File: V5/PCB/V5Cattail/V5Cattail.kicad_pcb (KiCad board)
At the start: 2 copper layers, 10.9 x 31.1 mm, 10 parts, among them U1 ST-0277D00-052-142, U2 SRV05-4_C558418, U3 BMI270

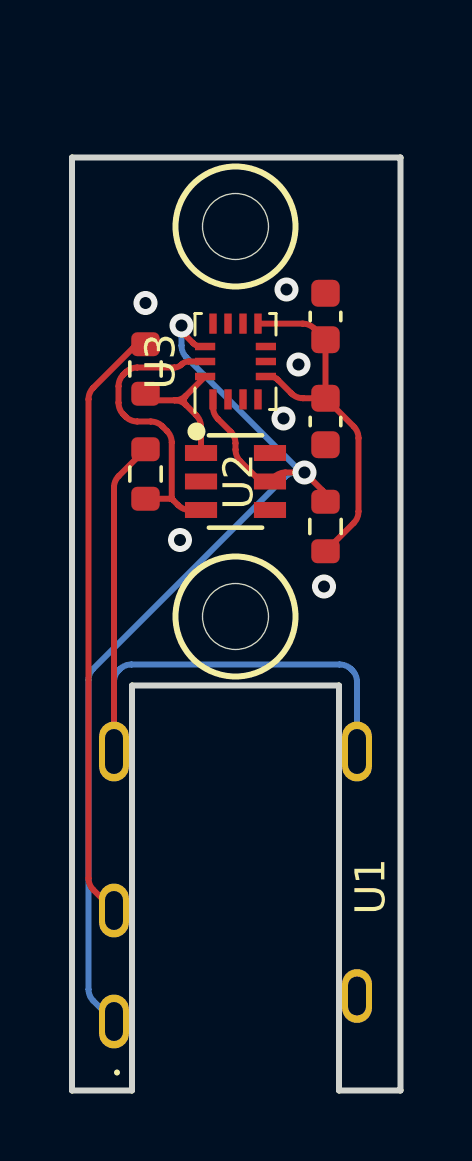
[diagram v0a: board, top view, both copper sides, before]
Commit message: reorganizing CAD files
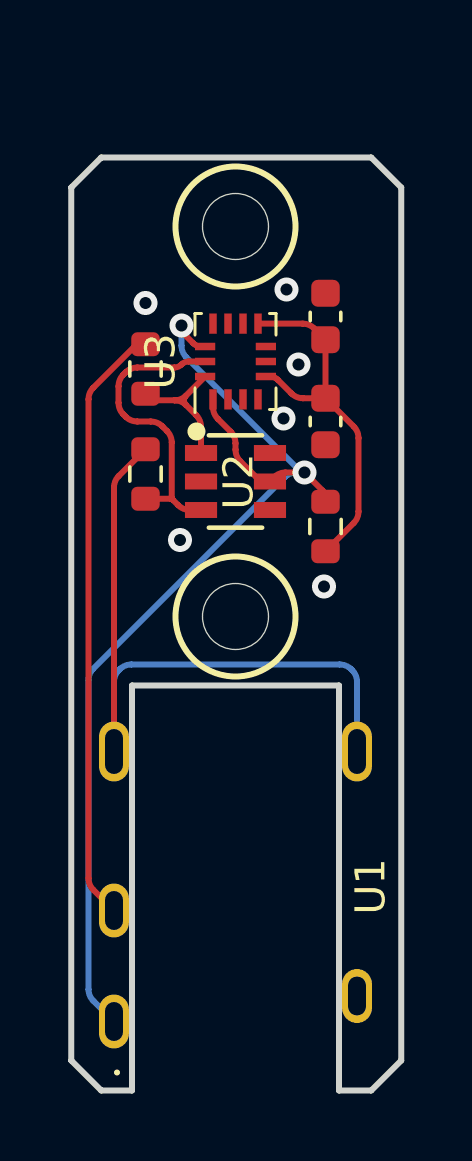
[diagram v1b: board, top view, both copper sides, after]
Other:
- board size 10.9 x 31.1 mm -> 11 x 31.1 mm
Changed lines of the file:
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@@
   (gr_circle (center 147 97) (end 148.99999 96.999991)
     (stroke (width 0.2) (type solid)) (fill none) (layer "F.SilkS"))
-  (gr_line (start 143.55 112.8) (end 143.55 99.3)
-    (stroke (width 0.2) (type default)) (layer "Edge.Cuts"))
-  (gr_line (start 150.45 112.8) (end 152.5 112.8)
-    (stroke (width 0.2) (type default)) (layer "Edge.Cuts"))
+  (gr_line (start 152.525 82.7) (end 151.525 81.7)
+    (stroke (width 0.2) (type solid)) (layer "Edge.Cuts"))
   (gr_line (start 143.55 112.8) (end 143.55 112.8)
     (stroke (width 0.2) (type default)) (layer "Edge.Cuts"))
-  (gr_line (start 141.55 112.8) (end 143.55 112.8)
-    (stroke (width 0.2) (type default)) (layer "Edge.Cuts"))
-  (gr_line (start 152.5 81.7) (end 141.55 81.7)
-    (stroke (width 0.2) (type default)) (layer "Edge.Cuts"))
-  (gr_line (start 150.45 99.3) (end 150.45 112.8)
-    (stroke (width 0.2) (type default)) (layer "Edge.Cuts"))
-  (gr_line (start 141.55 81.7) (end 141.55 112.8)
-    (stroke (width 0.2) (type default)) (layer "Edge.Cuts"))
+  (gr_line (start 141.525 111.8) (end 142.525 112.8)
+    (stroke (width 0.2) (type solid)) (layer "Edge.Cuts"))
+  (gr_line (start 142.525 81.7) (end 141.525 82.7)
+    (stroke (width 0.2) (type solid)) (layer "Edge.Cuts"))
   (gr_line (start 143.55 99.3) (end 150.45 99.3)
-    (stroke (width 0.2) (type default)) (layer "Edge.Cuts"))
-  (gr_line (start 152.5 112.8) (end 152.5 81.7)
-    (stroke (width 0.2) (type default)) (layer "Edge.Cuts"))
+    (stroke (width 0.2) (type solid)) (layer "Edge.Cuts"))
+  (gr_line (start 150.45 112.8) (end 150.45 99.3)
+    (stroke (width 0.2) (type solid)) (layer "Edge.Cuts"))
+  (gr_line (start 141.525 111.8) (end 141.525 82.7)
+    (stroke (width 0.2) (type solid)) (layer "Edge.Cuts"))
+  (gr_line (start 142.525 81.7) (end 151.525 81.7)
+    (stroke (width 0.2) (type solid)) (layer "Edge.Cuts"))
+  (gr_line (start 142.525 112.8) (end 143.55 112.8)
+    (stroke (width 0.2) (type solid)) (layer "Edge.Cuts"))
+  (gr_line (start 143.55 112.8) (end 143.55 99.3)
+    (stroke (width 0.2) (type solid)) (layer "Edge.Cuts"))
+  (gr_line (start 150.45 112.8) (end 151.525 112.8)
+    (stroke (width 0.2) (type solid)) (layer "Edge.Cuts"))
+  (gr_line (start 152.525 111.8) (end 152.525 82.7)
+    (stroke (width 0.2) (type solid)) (layer "Edge.Cuts"))
+  (gr_line (start 152.525 111.8) (end 151.525 112.8)
+    (stroke (width 0.2) (type solid)) (layer "Edge.Cuts"))
   (segment (start 147.747143 92.392551) (end 147.76534 92.392551) (width 0.2) (layer "F.Cu") (net 1))
   (segment (start 149.902772 92.802772) (end 149.3 92.2) (width 0.2) (layer "F.Cu") (net 1))
@@
     (polygon
       (pts
+        (xy 142.525 112.8)
+        (xy 141.525 111.8)
+        (xy 141.525 82.7)
+        (xy 142.525 81.7)
+        (xy 151.525 81.7)
+        (xy 152.525 82.7)
+        (xy 152.525 111.8)
+        (xy 151.525 112.8)
         (xy 150.45 112.8)
         (xy 150.45 99.3)
         (xy 143.55 99.3)
         (xy 143.55 112.8)
-        (xy 141.55 112.8)
-        (xy 141.55 81.7)
-        (xy 152.5 81.7)
-        (xy 152.5 112.8)
-      )
-    )
+      )
+    )

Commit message: Overdue backup
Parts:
- removed ? (x2): , 
- removed R1, R2, R3: 1k, Resistor_SMD:R_0603_1608Metric
- C1, C2: value 100n -> 100nF; footprint Capacitor_SMD:C_0603_1608Metric -> LilypadVR:C_0603_1608Metric
- J1: renamed from U1; value ST-0277D00-052-142 -> TRRS; footprint AUDIO-TH_ST-0277D00-052-142:AUDIO-TH_ST-0277D00-052-142 -> LilypadVR:AUDIO-TH_ST-0277D00-052-142
- U1: renamed from U2; footprint SOT-23-6_L2.9-W1.6-P0.95-LS2.8-BL:SOT-23-6_L2.9-W1.6-P0.95-LS2.8-BL -> LilypadVR:SOT-23-6
- moved C1 6.99 mm to (144.4, 86.3), turned to 90 degrees
- moved C2 3.67 mm to (147.0, 89.1), turned to 0 degrees
- moved U2 2.21 mm to (147.0, 86.3), turned to -90 degrees
- moved U1 0.70 mm to (147.0, 91.8), turned to 180 degrees
- renumbered U3 to U2
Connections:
- C1 pad 1: Net-(U3-VDD) -> GND
- C1 pad 2: GND -> +3V3
- C2 pad 1: Net-(U3-VDD) -> +3V3
- J1 pad 3: Net-(R1-Pad2) -> SDA
- J1 pad 4: Net-(R2-Pad2) -> SCL
- J1 pad 5: Net-(R2-Pad2) -> SCL
- U1 pad 1: /SDA -> SDA
- U1 pad 3: /SCL -> SCL
- U2 pad 13: /SCL -> SCL
- U2 pad 14: /SDA -> SDA
- U2 pad 5: Net-(U3-VDD) -> +3V3
- U2 pad 8: Net-(U3-VDD) -> +3V3
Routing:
- net SCL: track 0.00 -> 28.9 mm, vias 0 -> 1
- net SDA: track 0.00 -> 27.5 mm
- net Net-(R2-Pad2): track 23.9 -> 0.00 mm
- net Net-(R1-Pad2): track 20.1 -> 0.00 mm
- net Net-(U3-VDD): track 12.6 -> 0.00 mm
- net /SCL: track 10.2 -> 0.00 mm
- net +3V3: track 35.3 -> 43.7 mm, vias 2 -> 1
- net /SDA: track 4.89 -> 0.00 mm
- net GND: vias 6 -> 32
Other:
- board size 11 x 31.1 mm -> 11 x 34 mm
- rule pad_to_mask_clearance: 0 -> 0.038

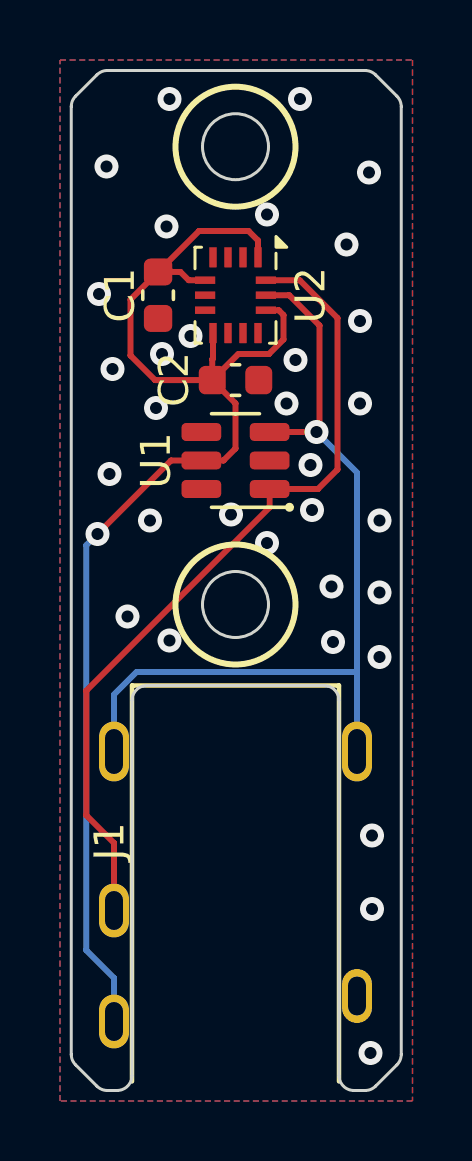
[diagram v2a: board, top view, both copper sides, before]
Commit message: Prototype Model/PCB Updates
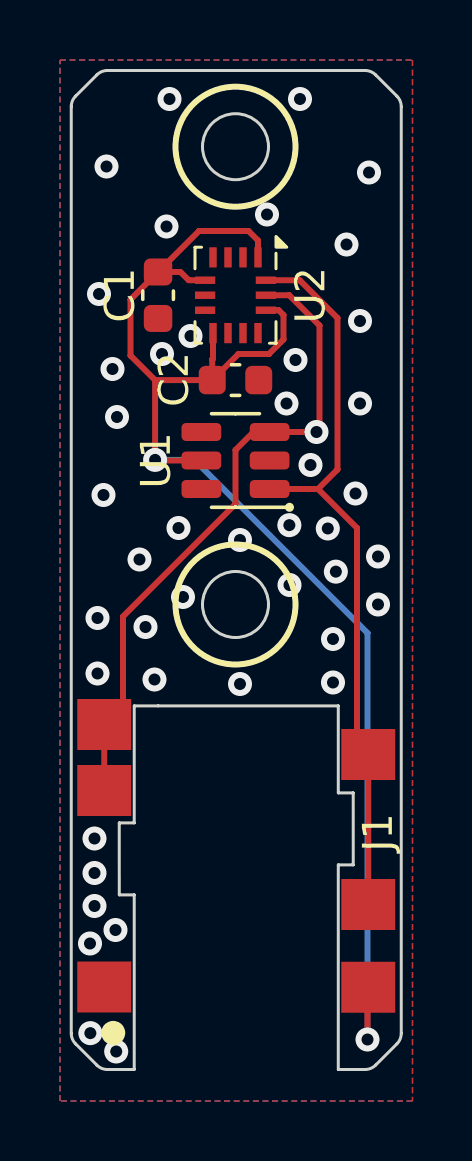
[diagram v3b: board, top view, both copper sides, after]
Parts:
- J1: footprint LilypadVR:AUDIO-TH_ST-0277D00-052-142 -> LilypadVR:AUDIO-SMD_PJ-342C
- moved J1 1.02 mm to (147.0, 105.0), turned to 180 degrees
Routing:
- net SCL: track 28.9 -> 21.9 mm
- net +3V3: track 43.7 -> 47.5 mm, vias 1 -> 2
- net SDA: track 27.5 -> 25.0 mm
- net GND: vias 32 -> 43
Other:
- board size 11 x 34 mm -> 11 x 33.3 mm
